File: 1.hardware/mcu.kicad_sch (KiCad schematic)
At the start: 52 parts, among them IC3 STWD100NXWY3F, J2 Conn_01x02, J3 Debug, Q1 PMOS, Q5 NMOS, Q6 NMOS, Q7 NMOS, SW2 SW_DPDT_x2, SW3 Reset_Btn, U1 STM32H743BITx, X1 SMD3225-4, Y1 X161032768KGD2SI

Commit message: 중간 저장
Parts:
- added C53, C54: 0.1uF/16V, symbol Device:C_Small_US
- added C55: 1uF/16V, symbol Device:C_Small_US
- added R139, R140: 0R/0.063w, symbol Device:R_Small_US
- added R141: 10K/0.063w, Resistor_SMD:R_0402_1005Metric, symbol Device:R_Small_US
- added R142: 120/0.1w, Resistor_SMD:R_0603_1608Metric, symbol Device:R_Small_US
- added U15: TL431AIDBZR, SamacSys_Parts:SOT95P237X112-3N, symbol SamacSys_Parts:TL431AIDBZR
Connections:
- net GND: now also C53.2, C54.2, C55.2, R141.2, U15.3 (ANODE)
- net MCU_VDD: now also U1.42 (VDDA), U1.6 (VBAT), C54.1, C55.1
- net USB_DM: now also R139.2; no longer U1.145 (PA11)
- net USB_DP: now also R140.2; no longer U1.146 (PA12)
- net at U1.197 (BOOT0): now also R141.1
- net ADC_VREF_2V5: now reaches U1.41 (VREF+)
- net ADC_VREF_2V5: now also C53.1, R142.2, U15.1 (CATHODE), U15.2 (REF)
- new net: R139.1, U1.145 (PA11)
- new net: R140.1, U1.146 (PA12)
- new net 3V3: R142.1
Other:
- moved on the sheet: C5, C7, J3, R111, X1

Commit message: 마이너 수정
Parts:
- added R143, R144: 10k/0.063w, symbol Device:R_Small_US
- added S1, S3: TSB008A2518A, SamacSys_Parts:TSB008A2518A, symbol SamacSys_Parts:TSB008A2518A
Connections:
- net 3V3_MCU: now also R143.2, R144.2
- net GND: now also S1.2 (NO), S3.2 (NO)
- new net BTN1: R143.1, S1.1 (COM)
- new net BTN2: R144.1, S3.1 (COM)

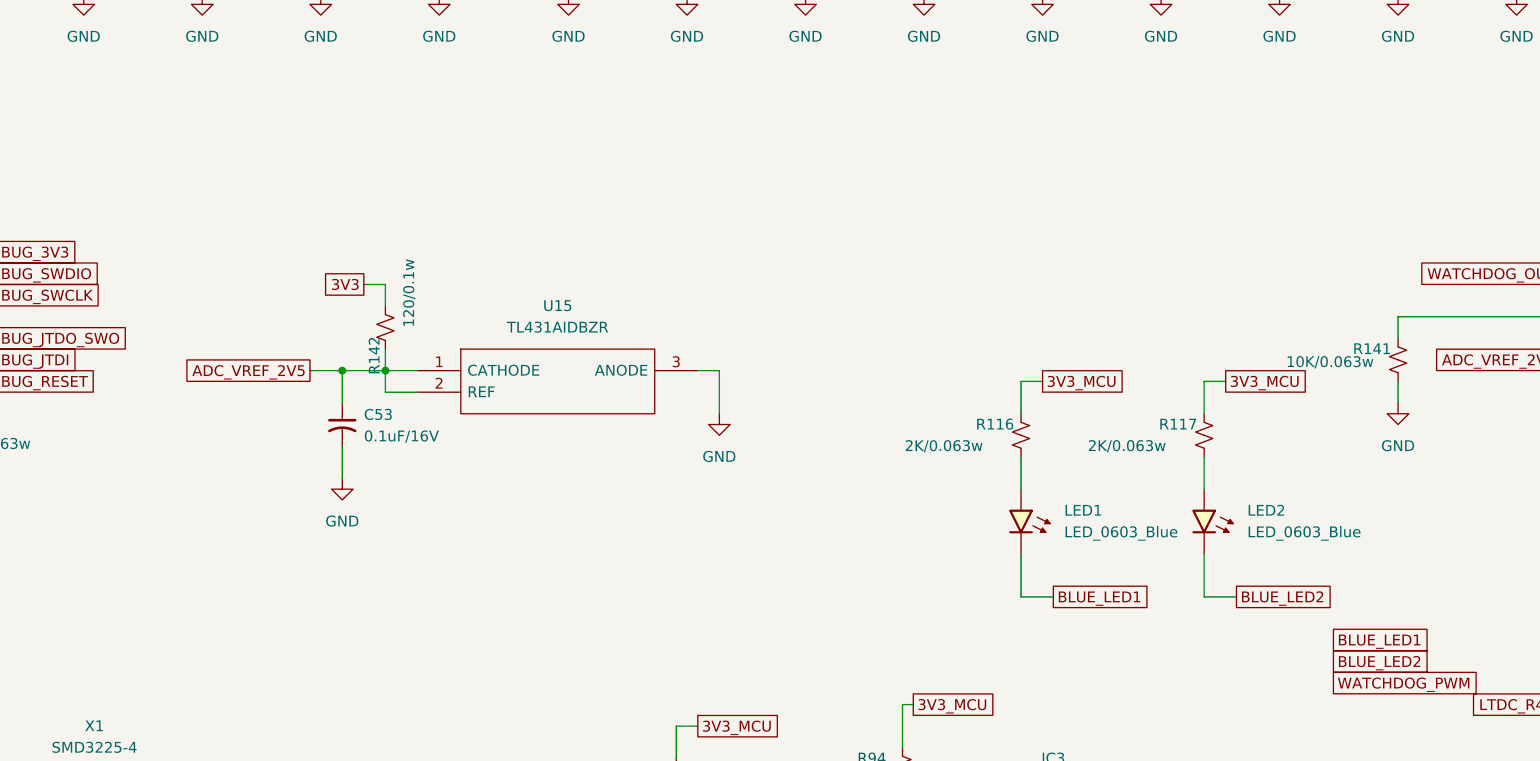
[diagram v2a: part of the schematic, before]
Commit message: mosfet 확정 및 드라이버 고려중 자세한 계산식 필요
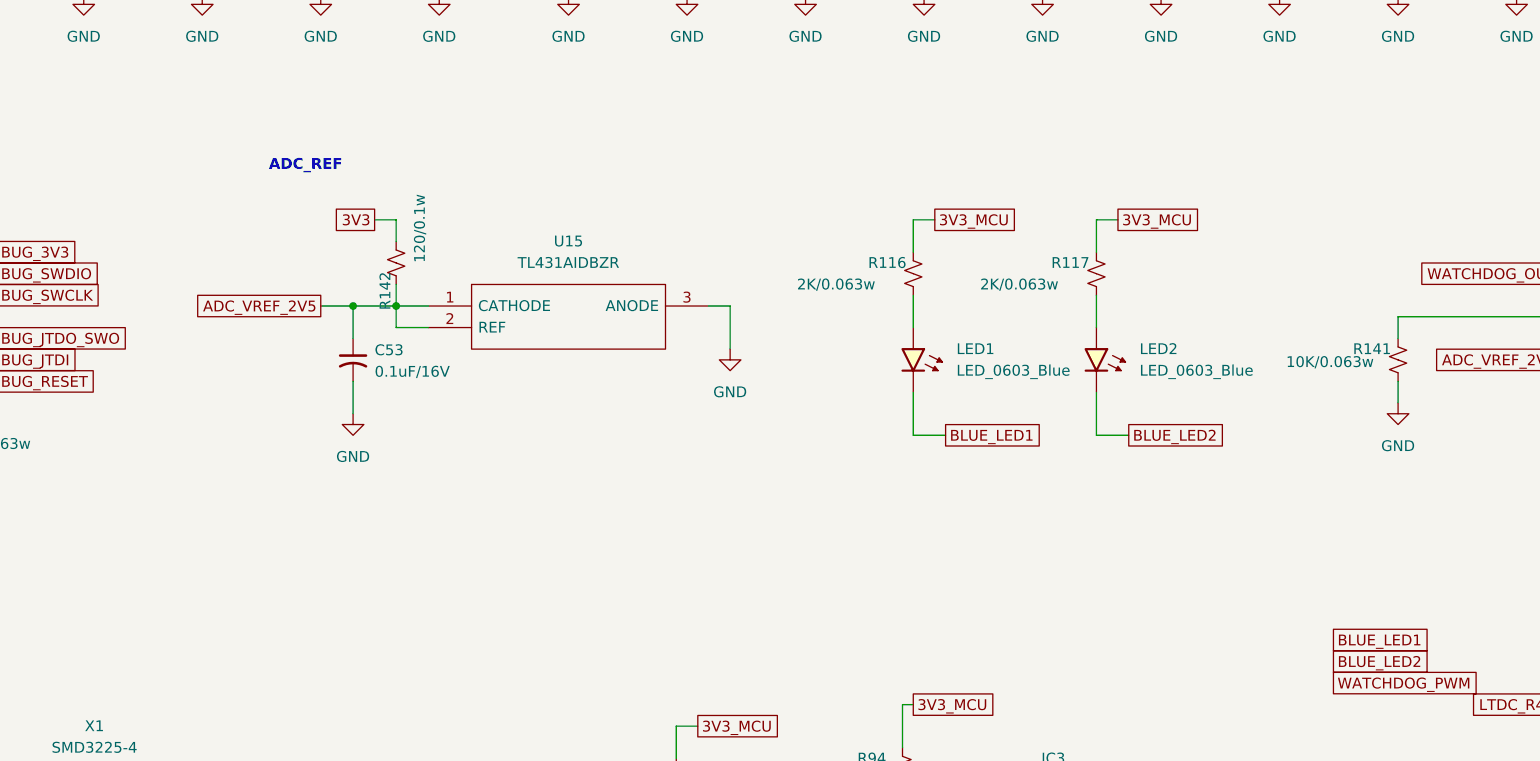
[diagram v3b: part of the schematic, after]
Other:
- note added: "ADC_REF"
- moved on the sheet: C53, LED1, LED2, R116, R117, R142, U15

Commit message: 중간 저장
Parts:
- removed J2: Conn_01x02, symbol Connector_Generic:Conn_01x02
- added C78: 1uF/16V, symbol Device:C_Small_US
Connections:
- net MCU_VDD is gone; now on net 3V3_MCU: C1.1, C10.1, C11.1, C12.1, C13.1, C14.1, C15.1, C16.1, C19.1, C2.1, C21.1, C3.1, C4.1, C54.1, C55.1, C6.1, C8.1, C9.1, U1.103 (VDD), U1.115 (VDD), U1.124 (VDD), U1.15 (VDD), U1.150 (VDD), U1.158 (VDD), U1.171 (VDD), U1.185 (VDD), U1.204 (VDD), U1.26 (VDD), U1.39 (VDD), U1.42 (VDDA), U1.52 (VDD), U1.59 (VDD), U1.6 (VBAT), U1.73 (VDD), U1.83 (VDD), U1.94 (VDD)
- net ADC_VREF_2V5: now also C78.1
- net GND: now also C78.2
- net HALL_A renamed HALL1_A
- net HALL_A_INTR renamed HALL1_A_INTR
- net HALL_B renamed HALL1_B
- net HALL_B_INTR renamed HALL1_B_INTR
- net HALL_C renamed HALL1_C
- net HALL_C_INTR renamed HALL1_C_INTR
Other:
- moved on the sheet: C5, C53, C7, J3, R111, R143, R144, S1, S3, X1

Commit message: 중간 저장
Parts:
- R116, R117: value 2K/0.063w -> 4.7k/0.063w
- R119, R120, R121, R122, R123, R124: value 2K/0.063w -> 2k/0.063w
- R94: value 4.7K/0.063w -> 4.7k/0.063w
- R96: value 10K/0.063w -> 10k/0.063w
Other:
- moved on the sheet: C68, C69, Y1

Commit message: 중간저장
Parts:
- added TP36: TP_2V5, symbol Connector:TestPoint
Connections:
- net ADC_VREF_2V5: now also TP36.1
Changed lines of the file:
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@@
+	)
+	(symbol
+		(lib_id "Connector:TestPoint")
+		(at 88.9 85.09 0)
+		(unit 1)
+		(exclude_from_sim no)
+		(in_bom yes)
+		(on_board yes)
+		(dnp no)
+		(fields_autoplaced yes)
+		(property "Reference" "TP36"
+			(at 91.44 80.5179 0)
+			(effects
+				(font
+					(size 1.27 1.27)
+				)
+				(justify left)
+			)
+		)
+		(property "Value" "TP_2V5"
+			(at 91.44 83.0579 0)
+			(effects
+				(font
+					(size 1.27 1.27)
+				)
+				(justify left)
+			)
+		)
+		(property "Footprint" ""
+			(at 93.98 85.09 0)
+			(effects
+				(font
+					(size 1.27 1.27)
+				)
+				(hide yes)
+			)
+		)
+		(property "Datasheet" "~"
+			(at 93.98 85.09 0)
+			(effects
+				(font
+					(size 1.27 1.27)
+				)
+				(hide yes)
+			)
+		)
+		(property "Description" "test point"
+			(at 88.9 85.09 0)
+			(effects
+				(font
+					(size 1.27 1.27)
+				)
+				(hide yes)
+			)
+		)
+		(pin "1"
+		)
+		(instances
+			(project "bldc_motor_controller"
+				(path "/a25adab6-a8c3-4e0e-8ba9-baac00aaa394/f1d28d97-f090-4298-9a06-d9576d5adbbf"
+					(reference "TP36")
+					(unit 1)
+				)
+			)
+		)
 	)
 	(symbol

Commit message: 중간 저장
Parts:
- added Q20: NMOS, symbol Simulation_SPICE:NMOS
- added R254, R255: 2k/0.063w, Resistor_SMD:R_0402_1005Metric, symbol Device:R_Small_US
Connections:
- net 3V3_MCU: now also Q20.2 (G), R254.1
- net 5V: now also R255.1
- net CAN_RXD: no longer U1.198 (PB8)
- net CAN_TXD: no longer U1.199 (PB9)
- net I2C1_SCL: no longer U1.195 (PB6)
- net I2C1_SDA: no longer U1.196 (PB7)
- net HALL1_A renamed HALL_A
- net HALL1_A_INTR renamed HALL_A_INTR
- net HALL1_B renamed HALL_B
- net HALL1_B_INTR renamed HALL_B_INTR
- net HALL1_C renamed HALL_C
- net HALL1_C_INTR renamed HALL_C_INTR
- new net HALL_6x_Pulse: Q20.3 (S), R254.2
- new net HALL_6x_Pulse_Sig_Follow: Q20.1 (D), R255.2
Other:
- moved on the sheet: C60, C61, C68, C69, D10, IC3, Q1, Q5, Q6, Q7, R110, R119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

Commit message: 중간 저장
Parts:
- removed Q20: NMOS, symbol Simulation_SPICE:NMOS
- removed R254, R255: 2k/0.063w, Resistor_SMD:R_0402_1005Metric, symbol Device:R_Small_US
